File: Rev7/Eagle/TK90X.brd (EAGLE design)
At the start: 217.8 x 132.1 mm, 224 parts, among them IC1 Z80, IC10 74LS244N, IC11 LM1886, IC12 LM1889, IC13 4116, IC14 4116, IC15 4116, IC16 4116, IC17 4116, IC18 4116, IC19 4116, IC2 ROM, IC20 4116, IC21 4416, IC22 4416, IC23 4416, IC24 4416, IC25 74LS00, IC26 74LS00, IC27 74LS32, IC28 74LS04, IC29 7805, IC3 ULA TK90, IC4 74LS74, IC5 74LS74, IC6 74LS157, IC7 74LS157, IC8 74LS157, IC9 74LS157, Q1 BC548, Q2 BC548, Q3 BF494, Q4 BC548, Q5 BD139, Q6 BD136, Q7 BC548, Q8 BC517, X1 POWER, X2 EAR, X3 MIC, X4 RCA, X5 RCA, X6 LED, X7 JOYSTICK

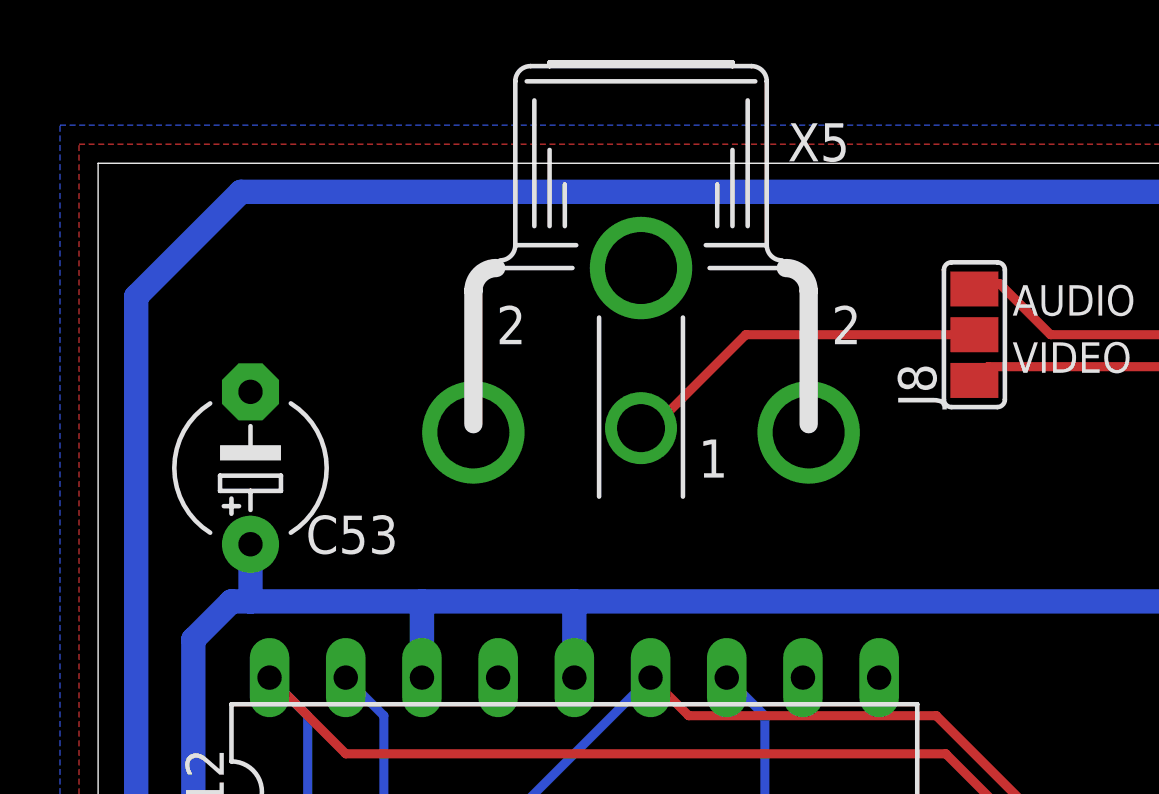
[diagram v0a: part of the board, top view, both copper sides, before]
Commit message: Corrigindo posição do conector RCA extra da Rev. 7 Adicionado conteúdo da EPROM Modificado lista de material de Excel para formato Markdown Melhorado documentações
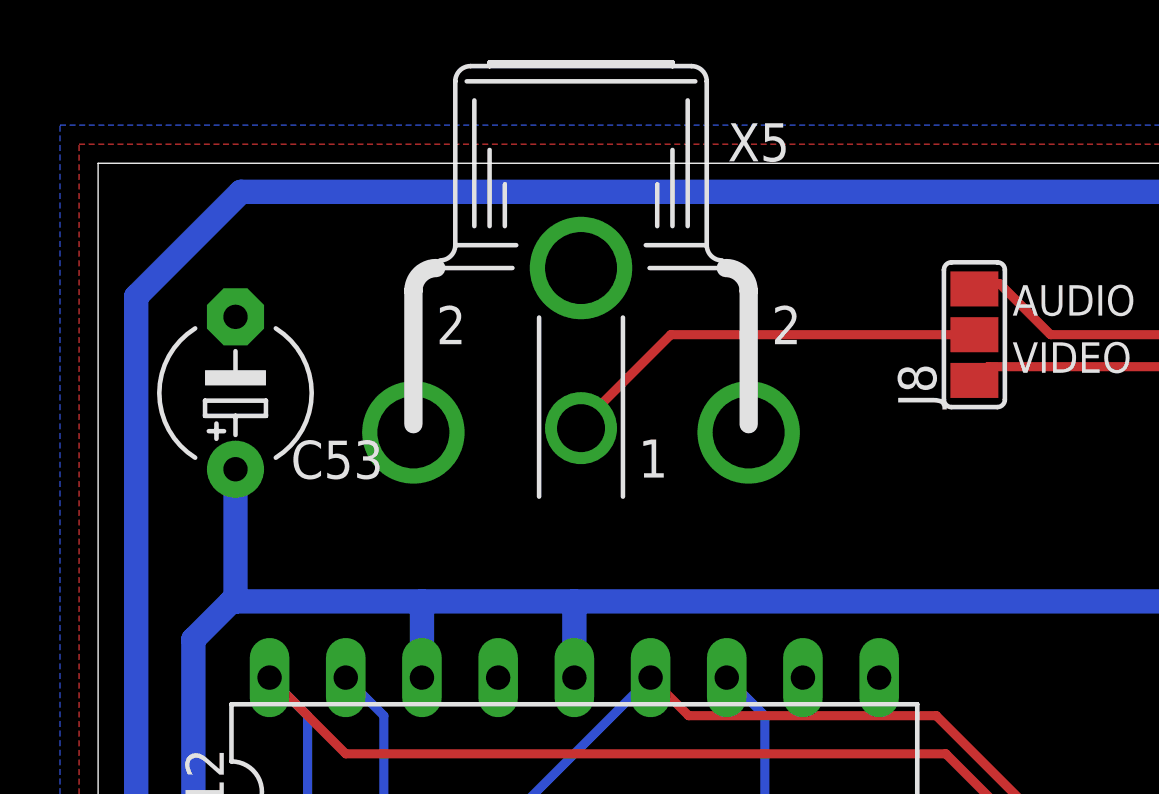
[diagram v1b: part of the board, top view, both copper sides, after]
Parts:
- moved C53 2.55 mm to (4.58, 124.4)
- moved X5 2.00 mm to (16.1, 126.0)
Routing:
- net +12V: track 330.5 -> 333.0 mm
- net N$74: track 12.4 -> 14.5 mm

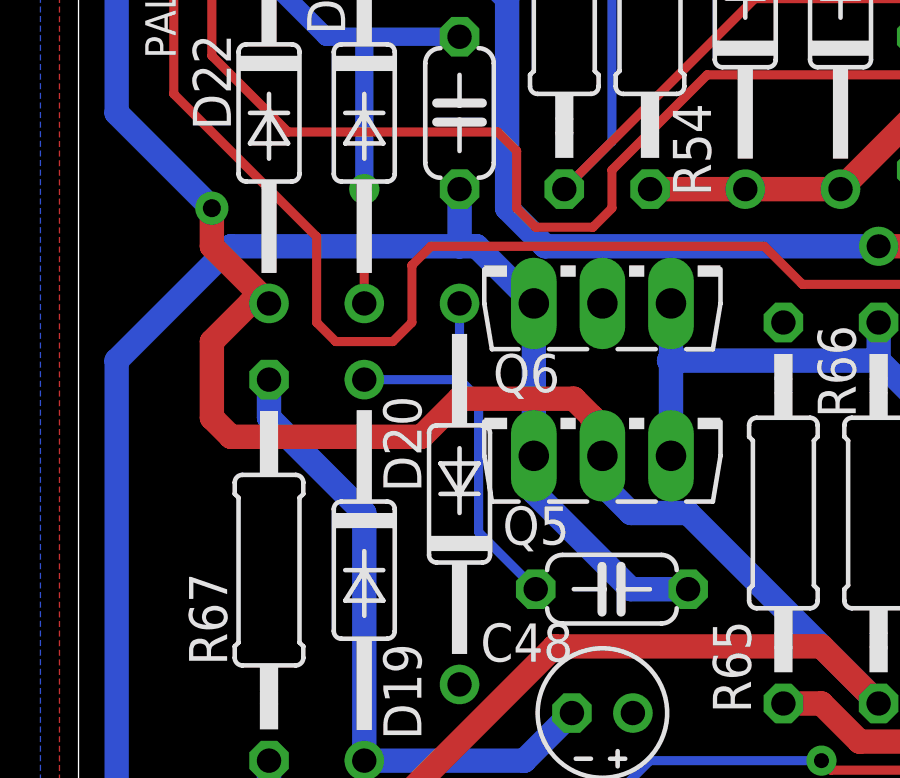
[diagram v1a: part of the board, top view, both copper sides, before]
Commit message: Corrigido valores de R68 e C52 para melhor geração dos 12V para o Vídeo e DRAMs. Corrigido largura de algumas trilhas
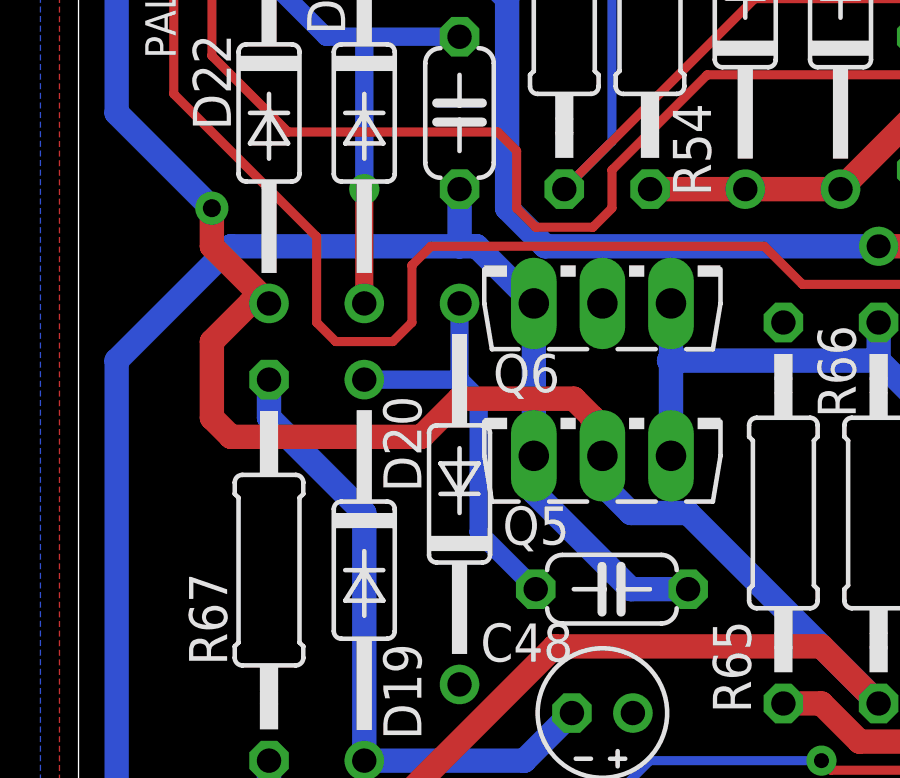
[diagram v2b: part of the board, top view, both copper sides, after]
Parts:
- C52: value 1u -> 10u
- R68: value 100 -> 33
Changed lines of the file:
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@@
 <setting verticaltext="up"/>
 </settings>
-<grid distance="0.5" unitdist="mm" unit="mm" style="lines" multiple="1" display="yes" altdistance="12.5" altunitdist="mil" altunit="mil"/>
+<grid distance="25" unitdist="mil" unit="mil" style="lines" multiple="1" display="yes" altdistance="12.5" altunitdist="mil" altunit="mil"/>
 <layers>
 <layer number="1" name="Top" color="4" fill="1" visible="yes" active="yes"/>
@@
 <attribute name="VALUE" x="14.5415" y="55.0545" size="1.27" layer="27" ratio="10" rot="R180"/>
 </element>
-<element name="C52" library="rcl" package="E2-4" value="1u" x="13.0175" y="89.8525" smashed="yes" rot="R90">
+<element name="C52" library="rcl" package="E2-4" value="10u" x="13.0175" y="89.8525" smashed="yes" rot="R90">
 <attribute name="NAME" x="12.065" y="92.7735" size="1.27" layer="25" ratio="10"/>
 <attribute name="VALUE" x="11.1125" y="86.4235" size="1.27" layer="27" ratio="10"/>
@@
 <attribute name="VALUE" x="7.0358" y="41.529" size="1.27" layer="27" ratio="10" rot="R90"/>
 </element>
-<element name="R68" library="rcl" package="0207/12" value="100" x="9.525" y="73.66" smashed="yes" rot="R90">
+<element name="R68" library="rcl" package="0207/12" value="33" x="9.525" y="73.66" smashed="yes" rot="R90">
 <attribute name="NAME" x="8.763" y="76.835" size="1.27" layer="25" ratio="10" rot="R90"/>
 <attribute name="VALUE" x="10.2108" y="72.3265" size="1.27" layer="27" ratio="10" rot="R90"/>
@@
 <contactref element="D19" pad="C"/>
 <contactref element="D20" pad="A"/>
-<wire x1="9.525" y1="49.53" x2="12.7" y2="49.53" width="0.3048" layer="16"/>
-<wire x1="12.7" y1="49.53" x2="13.335" y2="48.895" width="0.3048" layer="16"/>
-<wire x1="13.335" y1="48.895" x2="13.335" y2="44.45" width="0.3048" layer="16"/>
-<wire x1="13.335" y1="44.45" x2="15.24" y2="42.545" width="0.3048" layer="16"/>
-<wire x1="12.7" y1="52.07" x2="12.7" y2="49.53" width="0.3048" layer="16"/>
+<wire x1="9.525" y1="49.53" x2="12.7" y2="49.53" width="0.6096" layer="16"/>
+<wire x1="12.7" y1="49.53" x2="13.335" y2="48.895" width="0.6096" layer="16"/>
+<wire x1="13.335" y1="48.895" x2="13.335" y2="44.45" width="0.6096" layer="16"/>
+<wire x1="13.335" y1="44.45" x2="15.24" y2="42.545" width="0.6096" layer="16"/>
+<wire x1="12.7" y1="52.07" x2="12.7" y2="49.53" width="0.6096" layer="16"/>
 </signal>
 <signal name="N$43">
@@
 <wire x1="9.525" y1="60.96" x2="9.525" y2="55.88" width="0.6096" layer="16"/>
 <via x="9.525" y="55.88" extent="1-16" drill="0.5"/>
-<wire x1="9.525" y1="55.88" x2="9.525" y2="52.07" width="0.3048" layer="1"/>
+<wire x1="9.525" y1="55.88" x2="9.525" y2="52.07" width="0.6096" layer="1"/>
 </signal>
 <signal name="N$52">

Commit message: Adicionado Interactive BOM para a Revisão 7
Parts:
- U$1: value TK90_EDGE -> (none)
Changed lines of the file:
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@@
 <?xml version="1.0" encoding="utf-8"?>
 <!DOCTYPE eagle SYSTEM "eagle.dtd">
-<eagle version="9.5.1">
+<eagle version="9.6.2">
 <drawing>
 <settings>
@@
 <attribute name="NAME" x="107.696" y="65.7225" size="1.27" layer="25" ratio="10" rot="R180"/>
 <attribute name="POPULARITY" value="0" x="106.68" y="66.9925" size="1.778" layer="27" rot="R180" display="off"/>
+<attribute name="TP_SIGNAL_NAME" value="" x="107.95" y="69.5325" size="1" layer="37" rot="R180"/>
 <attribute name="TP_SIGNAL_NAME" value="" x="106.68" y="66.9925" size="1.778" layer="27" rot="R180" display="off"/>
-<attribute name="TP_SIGNAL_NAME" value="" x="107.95" y="69.5325" size="1" layer="37" rot="R180"/>
 <attribute name="VALUE" x="106.68" y="66.9925" size="0.0254" layer="27" rot="R180"/>
 </element>
@@
 <attribute name="NAME" x="149.7965" y="116.84" size="1.27" layer="25" ratio="10"/>
 <attribute name="POPULARITY" value="0" x="153.035" y="119.38" size="1.778" layer="27" rot="R180" display="off"/>
+<attribute name="TP_SIGNAL_NAME" value="" x="154.305" y="121.92" size="1" layer="37" rot="R180"/>
 <attribute name="TP_SIGNAL_NAME" value="" x="153.035" y="119.38" size="1.778" layer="27" rot="R180" display="off"/>
-<attribute name="TP_SIGNAL_NAME" value="" x="154.305" y="121.92" size="1" layer="37" rot="R180"/>
 <attribute name="VALUE" x="153.035" y="119.38" size="0.0254" layer="27" rot="R180"/>
 </element>
@@
 <attribute name="NAME" x="91.821" y="4.7625" size="1.27" layer="25" ratio="10" rot="R180"/>
 <attribute name="POPULARITY" value="0" x="90.17" y="6.35" size="1.778" layer="27" rot="R180" display="off"/>
+<attribute name="TP_SIGNAL_NAME" value="" x="91.44" y="8.89" size="1" layer="37" rot="R180"/>
 <attribute name="TP_SIGNAL_NAME" value="" x="90.17" y="6.35" size="1.778" layer="27" rot="R180" display="off"/>
-<attribute name="TP_SIGNAL_NAME" value="" x="91.44" y="8.89" size="1" layer="37" rot="R180"/>
 <attribute name="VALUE" x="90.17" y="6.35" size="0.0254" layer="27" rot="R180"/>
 </element>
@@
 <attribute name="NAME" x="84.201" y="4.7625" size="1.27" layer="25" ratio="10" rot="R180"/>
 <attribute name="POPULARITY" value="0" x="82.55" y="6.35" size="1.778" layer="27" rot="R180" display="off"/>
+<attribute name="TP_SIGNAL_NAME" value="" x="83.82" y="8.89" size="1" layer="37" rot="R180"/>
 <attribute name="TP_SIGNAL_NAME" value="" x="82.55" y="6.35" size="1.778" layer="27" rot="R180" display="off"/>
-<attribute name="TP_SIGNAL_NAME" value="" x="83.82" y="8.89" size="1" layer="37" rot="R180"/>
 <attribute name="VALUE" x="82.55" y="6.35" size="0.0254" layer="27" rot="R180"/>
 </element>
@@
 <attribute name="NAME" x="88.011" y="4.7625" size="1.27" layer="25" ratio="10" rot="R180"/>
 <attribute name="POPULARITY" value="0" x="86.36" y="6.35" size="1.778" layer="27" rot="R180" display="off"/>
+<attribute name="TP_SIGNAL_NAME" value="" x="87.63" y="8.89" size="1" layer="37" rot="R180"/>
 <attribute name="TP_SIGNAL_NAME" value="" x="86.36" y="6.35" size="1.778" layer="27" rot="R180" display="off"/>
-<attribute name="TP_SIGNAL_NAME" value="" x="87.63" y="8.89" size="1" layer="37" rot="R180"/>
 <attribute name="VALUE" x="86.36" y="6.35" size="0.0254" layer="27" rot="R180"/>
 </element>
@@
 <attribute name="NAME" x="40.7035" y="45.72" size="1.27" layer="25" ratio="10" rot="R180"/>
 <attribute name="POPULARITY" value="0" x="39.6875" y="46.99" size="1.778" layer="27" rot="R180" display="off"/>
+<attribute name="TP_SIGNAL_NAME" value="" x="40.9575" y="49.53" size="1" layer="37" rot="R180"/>
 <attribute name="TP_SIGNAL_NAME" value="" x="39.6875" y="46.99" size="1.778" layer="27" rot="R180" display="off"/>
-<attribute name="TP_SIGNAL_NAME" value="" x="40.9575" y="49.53" size="1" layer="37" rot="R180"/>
 <attribute name="VALUE" x="39.6875" y="46.99" size="0.0254" layer="27" rot="R180"/>
 </element>
@@
 <attribute name="NAME" x="101.219" y="77.7875" size="1.27" layer="25" ratio="10"/>
 <attribute name="POPULARITY" value="0" x="102.87" y="80.645" size="1.778" layer="27" display="off"/>
+<attribute name="TP_SIGNAL_NAME" value="" x="101.6" y="78.105" size="1" layer="37"/>
 <attribute name="TP_SIGNAL_NAME" value="" x="102.87" y="80.645" size="1.778" layer="27" display="off"/>
-<attribute name="TP_SIGNAL_NAME" value="" x="101.6" y="78.105" size="1" layer="37"/>
 <attribute name="VALUE" x="102.87" y="80.645" size="0.0254" layer="27"/>
 </element>
-<element name="U$1" library="tk90" package="TK-EDGE" value="TK90_EDGE" x="131.445" y="128.27" smashed="yes"/>
+<element name="U$1" library="tk90" package="TK-EDGE" value="" x="131.445" y="128.27" smashed="yes"/>
 <element name="X2" library="tk90" package="P2S" value="EAR" x="61.595" y="123.825" smashed="yes" rot="R180">
 <attribute name="MODEL" value="PJ-301A" x="61.595" y="123.825" size="1.778" layer="27" rot="R180" display="off"/>
@@
 <attribute name="NAME" x="73.914" y="100.6475" size="1.27" layer="25" ratio="10"/>
 <attribute name="POPULARITY" value="0" x="73.025" y="103.1875" size="1.778" layer="27" display="off"/>
+<attribute name="TP_SIGNAL_NAME" value="" x="71.755" y="100.6475" size="1" layer="37"/>
 <attribute name="TP_SIGNAL_NAME" value="" x="73.025" y="103.1875" size="1.778" layer="27" display="off"/>
-<attribute name="TP_SIGNAL_NAME" value="" x="71.755" y="100.6475" size="1" layer="37"/>
 <attribute name="VALUE" x="73.025" y="103.1875" size="0.0254" layer="27"/>
 </element>
@@
 <attribute name="NAME" x="187.6425" y="55.499" size="1.27" layer="25" ratio="10" rot="R90"/>
 <attribute name="POPULARITY" value="0" x="184.785" y="57.15" size="1.778" layer="27" display="off"/>
+<attribute name="TP_SIGNAL_NAME" value="" x="183.515" y="54.61" size="1" layer="37"/>
 <attribute name="TP_SIGNAL_NAME" value="" x="184.785" y="57.15" size="1.778" layer="27" display="off"/>
-<attribute name="TP_SIGNAL_NAME" value="" x="183.515" y="54.61" size="1" layer="37"/>
 <attribute name="VALUE" x="184.785" y="57.15" size="0.0254" layer="27"/>
 </element>
@@
 <attribute name="NAME" x="31.369" y="70.32625" size="1.27" layer="25" font="vector" ratio="10"/>
 <attribute name="POPULARITY" value="0" x="33.9725" y="68.58" size="1.778" layer="27" display="off"/>
+<attribute name="TP_SIGNAL_NAME" value="" x="32.7025" y="66.04" size="1" layer="37"/>
 <attribute name="TP_SIGNAL_NAME" value="" x="33.9725" y="68.58" size="1.778" layer="27" display="off"/>
-<attribute name="TP_SIGNAL_NAME" value="" x="32.7025" y="66.04" size="1" layer="37"/>
 <attribute name="VALUE" x="33.9725" y="68.58" size="0.0254" layer="27"/>
 </element>
